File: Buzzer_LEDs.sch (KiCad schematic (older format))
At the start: 15 parts, among them Q1 2N7002BK, Q2 BS250P

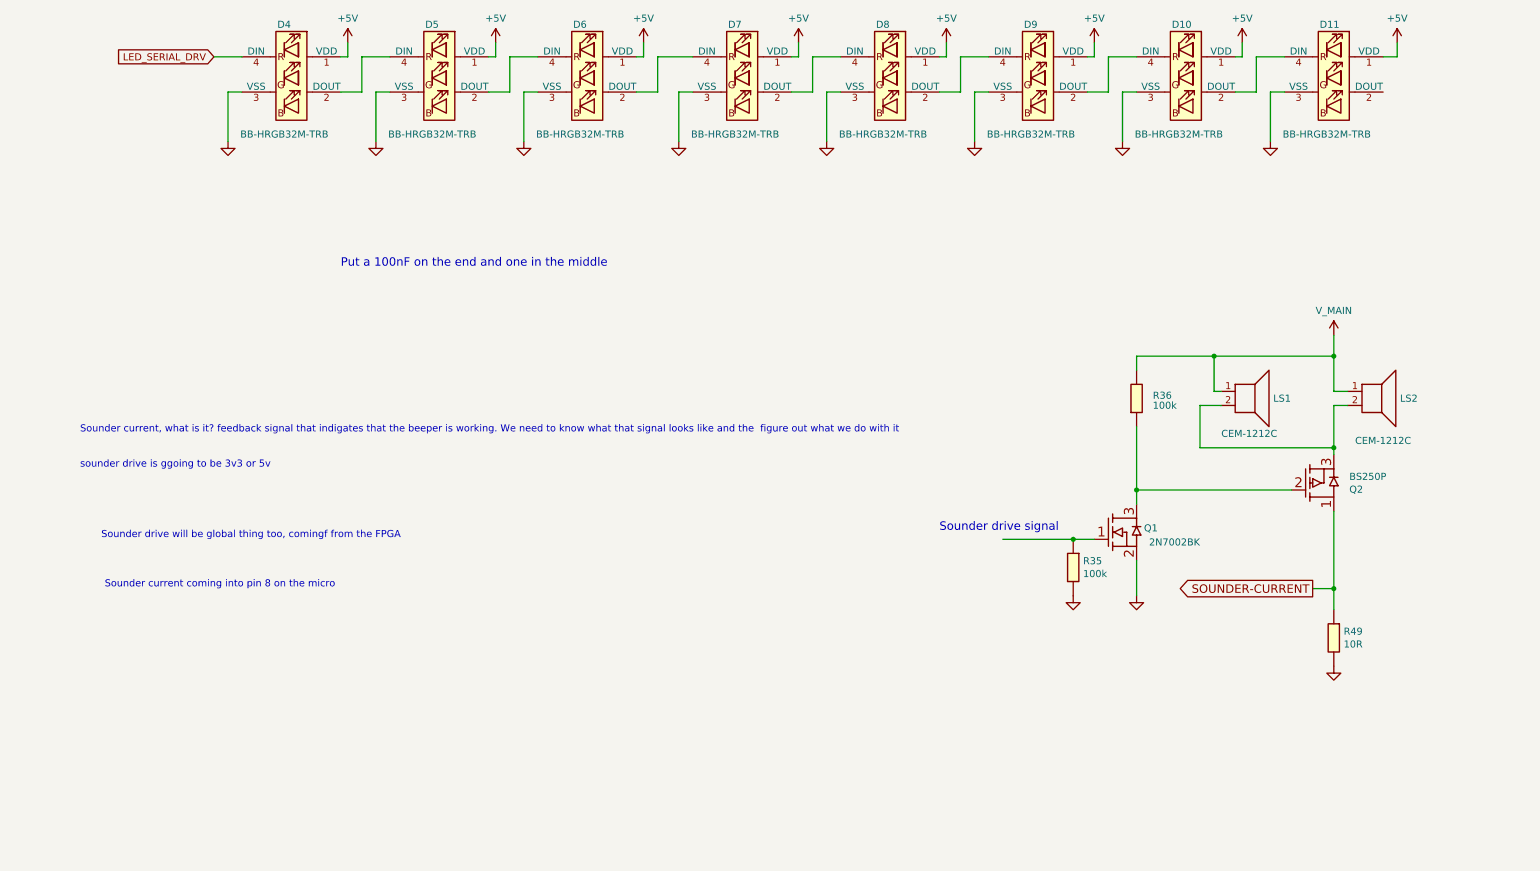
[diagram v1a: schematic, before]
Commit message: Buzzer drive circuit and oxygen sensor connector
this branch has add a 3 pin connector for oxygen sensor. it also has a drive circuit for a buzzer. the input signal needs to be confirmed.
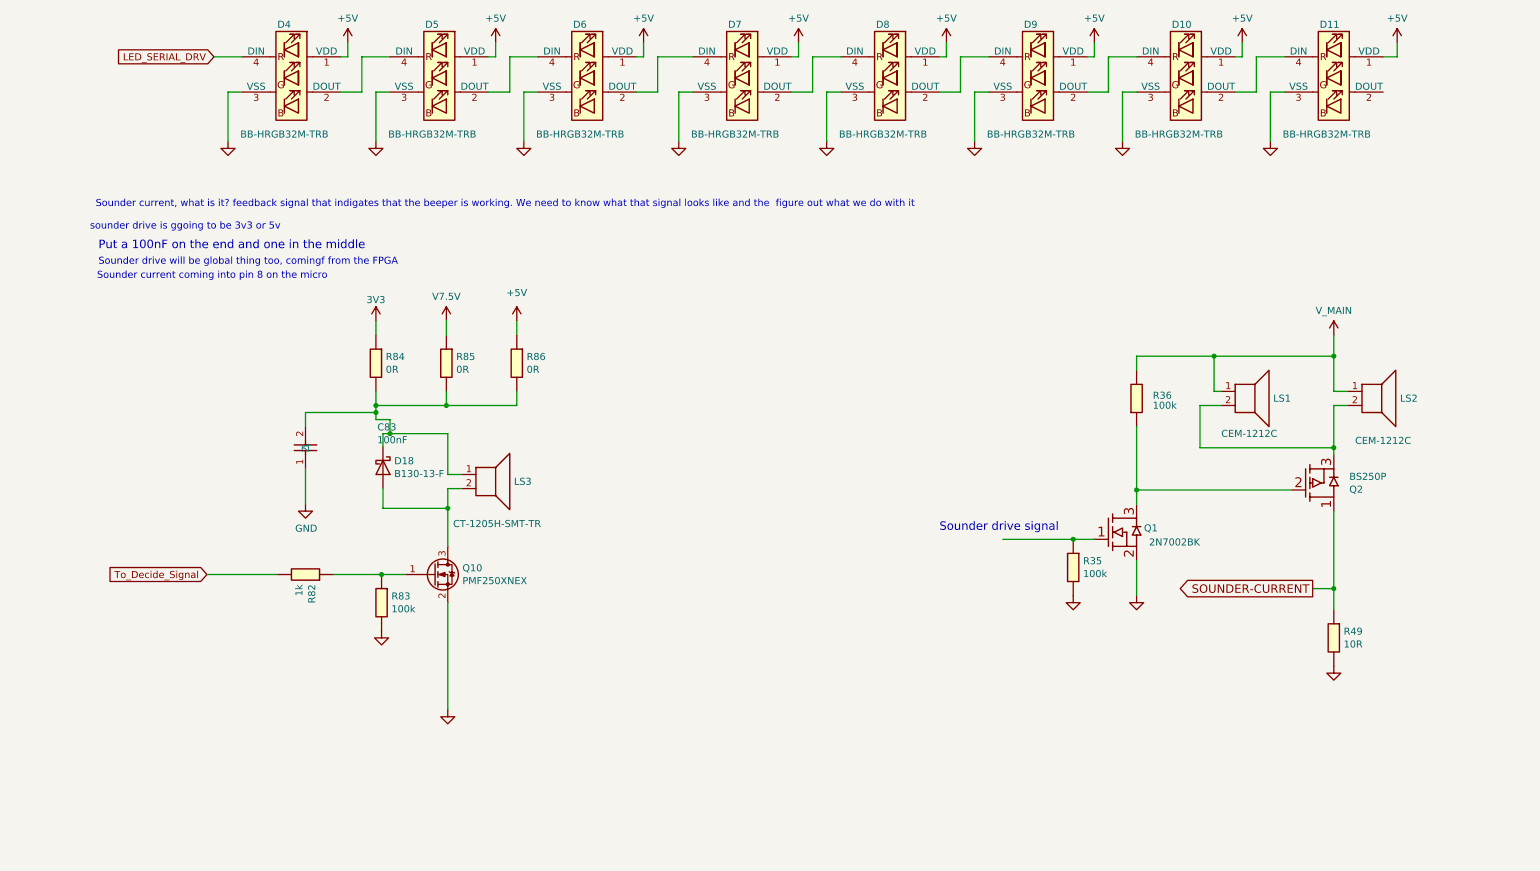
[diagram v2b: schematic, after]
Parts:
- added C83: 100nF_0603_Ceramic_Capacitor,_10%,_X7R,_25V, Capacitor_SMD:C_0201_0603Metric, symbol OpenVent:100nF_0603_Ceramic_Capacitor,_10%,_X7R,_25V
- added D18: B130-13-F, Diode_SMD:D_SMA, symbol Diode:BAT43W-V
- added LS3: MAGNETIC_BUZZER_TRANSDUCER, OpenVent_Buzzer:rrrr, symbol OpenVent-rescue:AUDIO_MAGNETIC_INDICATOR-Device
- added Q10: PMF250XNEX, Package_TO_SOT_SMD:SOT-323_SC-70, symbol Transistor_FET:DMN3042L
- added R82: 1K_0603_Chip_Resistor,_1%,_0.1W, Resistor_SMD:R_0603_1608Metric, symbol OpenVent:100K_0603_Chip_Resistor,_1%,_0.1W
- added R83: 100K_0603_Chip_Resistor,_1%,_0.1W, Resistor_SMD:R_0603_1608Metric, symbol OpenVent:100K_0603_Chip_Resistor,_1%,_0.1W
- added R84, R85, R86: 0R_0603_Chip_Resistor,_1%,_0.1W, Resistor_SMD:R_0603_1608Metric, symbol OpenVent:100K_0603_Chip_Resistor,_1%,_0.1W
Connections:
- net +5V: now also R85.1, R86.1
- net GND: now also C83.1, Q10.2 (S), R83.2
- new net: Q10.1 (G), R82.1, R83.1
- new net: C83.2, D18.1 (K), LS3.1, R84.2, R85.2, R86.2
- new net: D18.2 (A), LS3.2, Q10.3 (D)
- new net +3V3: R84.1
- new net To_Decide_Signal: R82.2

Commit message: added speaker drive
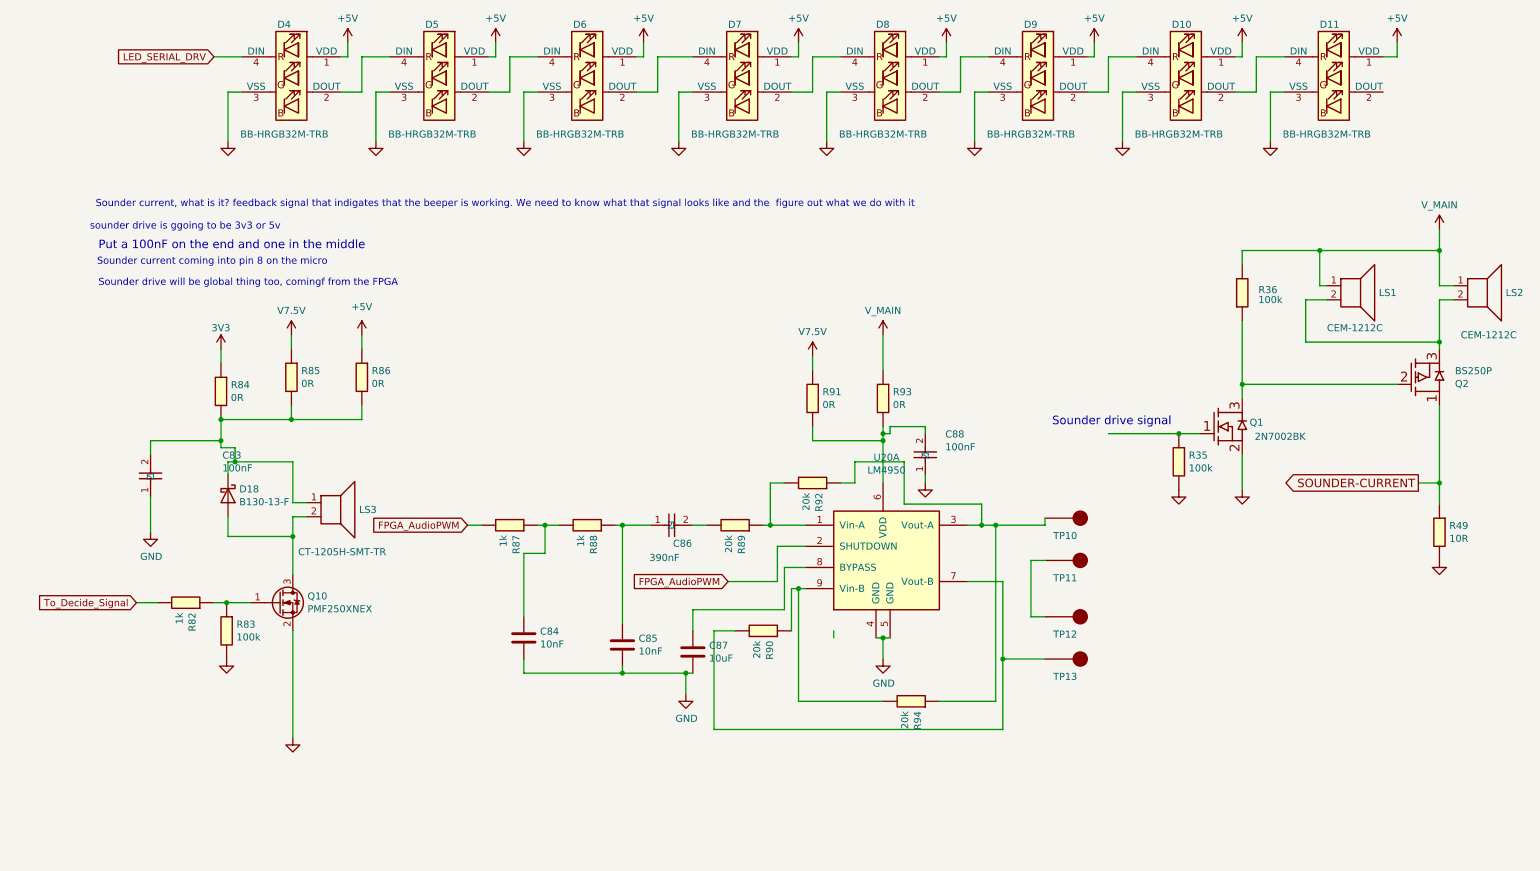
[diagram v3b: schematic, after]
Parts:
- added C84, C85: 10nF, symbol Device:C
- added C86: 390nF_0603_Ceramic_Capacitor,_10%,_X7R,_25V, Capacitor_SMD:C_0201_0603Metric, symbol OpenVent:100nF_0603_Ceramic_Capacitor,_10%,_X7R,_25V
- added C87: 10uF, symbol Device:C
- added C88: 100nF_0603_Ceramic_Capacitor,_10%,_X7R,_25V, Capacitor_SMD:C_0201_0603Metric, symbol OpenVent:100nF_0603_Ceramic_Capacitor,_10%,_X7R,_25V
- added R87, R88: 1K_0603_Chip_Resistor,_1%,_0.1W, Resistor_SMD:R_0603_1608Metric, symbol OpenVent:100K_0603_Chip_Resistor,_1%,_0.1W
- added R89, R90, R92, R94: 20K_0603_Chip_Resistor,_1%,_0.1W, Resistor_SMD:R_0603_1608Metric, symbol OpenVent:100K_0603_Chip_Resistor,_1%,_0.1W
- added R91, R93: 0R_0603_Chip_Resistor,_1%,_0.1W, Resistor_SMD:R_0603_1608Metric, symbol OpenVent:100K_0603_Chip_Resistor,_1%,_0.1W
- added TP10, TP11, TP12, TP13: Test_Point_PTH, symbol OpenVent:Test_Point_PTH
- added U20: LM4950, OpenVent_Buzzer:LM4950_FP, symbol OpenVent:LM4950
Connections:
- net +5V: now also R91.1, R93.1
- net GND: now also C84.2, C85.2, C87.2, C88.1, U20.4 (GND), U20.5 (GND)
- new net: R89.1, R92.2, U20.1 (Vin-A)
- new net: R92.1, R94.1, TP10.1, U20.3 (Vout-A)
- new net: C88.2, R91.2, R93.2, U20.6 (VDD)
- new net: R90.2, TP13.1, U20.7 (Vout-B)
- new net: C87.1, U20.8 (BYPASS)
- new net: R90.1, R94.2, U20.9 (Vin-B)
- new net: TP11.1, TP12.1
- new net: C86.2, R89.2
- new net: C85.1, C86.1, R88.1
- new net: C84.1, R87.1, R88.2
- new net FPGA_AudioPWM: R87.2, U20.2 (SHUTDOWN)
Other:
- moved on the sheet: C83, D18, LS1, LS2, LS3, Q1, Q10, Q2, R35, R36, R49, R82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

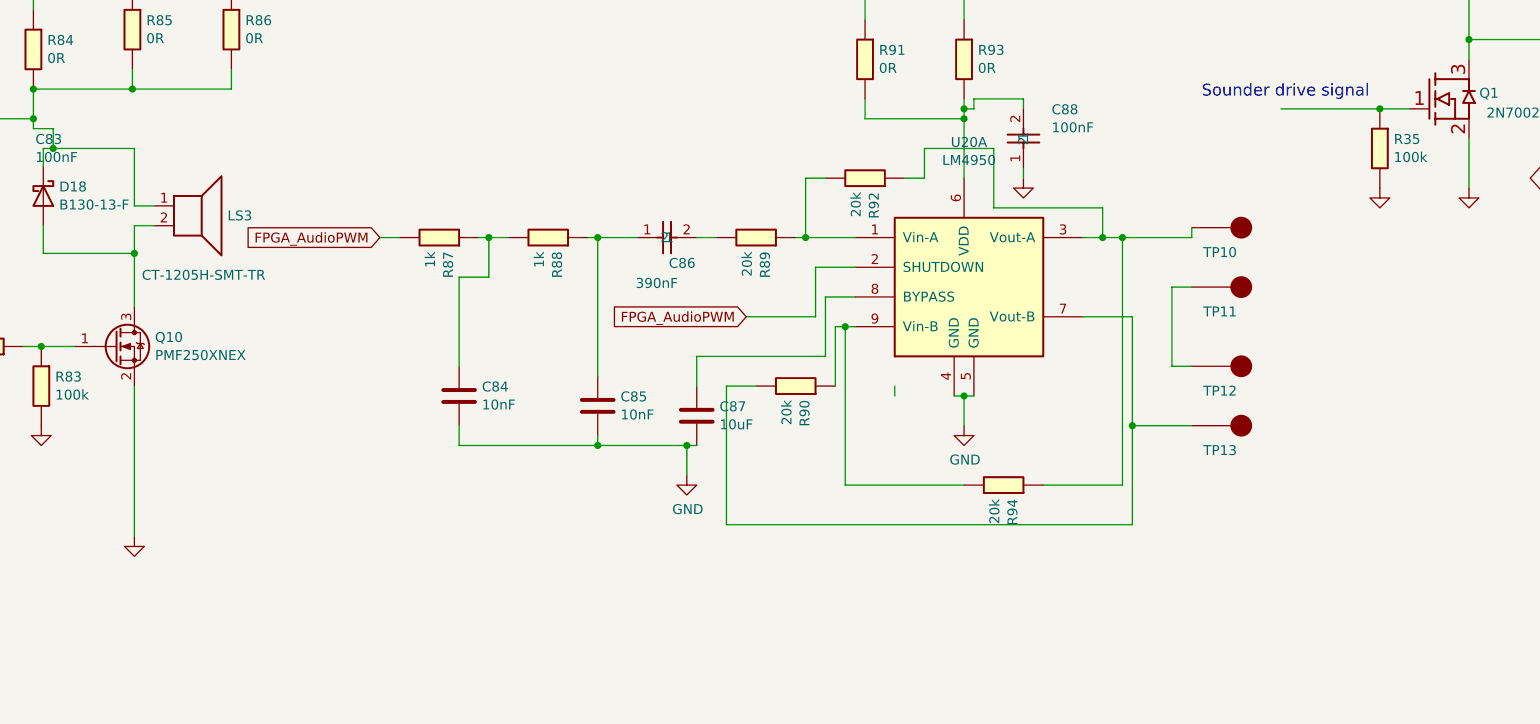
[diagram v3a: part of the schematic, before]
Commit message: add volume for speaker
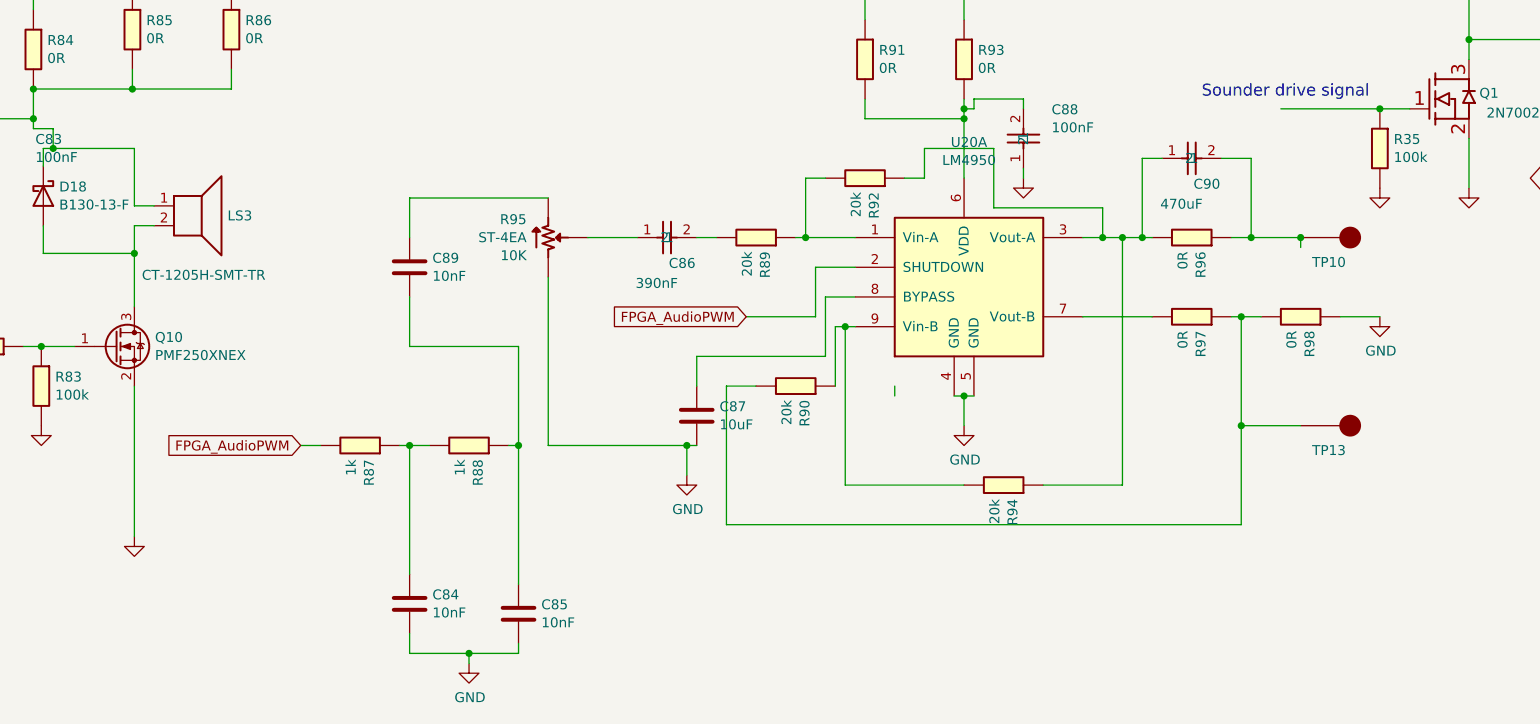
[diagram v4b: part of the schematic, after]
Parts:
- removed TP11, TP12: Test_Point_PTH, symbol OpenVent:Test_Point_PTH
- added C89: 10nF, symbol Device:C
- added C90: 470uF_0603_Ceramic_Capacitor,_10%,_X7R,_25V, Capacitor_SMD:C_0201_0603Metric, symbol OpenVent:100nF_0603_Ceramic_Capacitor,_10%,_X7R,_25V
- added R95: ST-4EA, OpenVent_Buzzer:ST_4EA, symbol OpenVent:Potentiometer
- added R96, R97, R98: 0R_0603_Chip_Resistor,_1%,_0.1W, Resistor_SMD:R_0603_1608Metric, symbol OpenVent:100K_0603_Chip_Resistor,_1%,_0.1W
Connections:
- net GND: now also R95.1, R98.1
- net at R92.1, R94.1, U20.3 (Vout-A): now also C90.1, R96.2; no longer TP10.1
- net at R90.2, TP13.1: now also R97.1, R98.2; no longer U20.7 (Vout-B)
- net at C85.1, R88.1: now also C89.2; no longer C86.1
- new net: R97.2, U20.7 (Vout-B)
- new net: C90.2, R96.1, TP10.1
- new net: C86.1, R95.2
- new net: C89.1, R95.3
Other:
- moved on the sheet: C84, C85, R87, R88, TP10, TP13
